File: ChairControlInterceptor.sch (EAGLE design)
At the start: 22 parts, among them J1 Digital_0_7, J2 Analog, J3 Digital_8_13, SW1 TL46WO, X1 INPUT, X2 OUTPUT, X4 INPUT

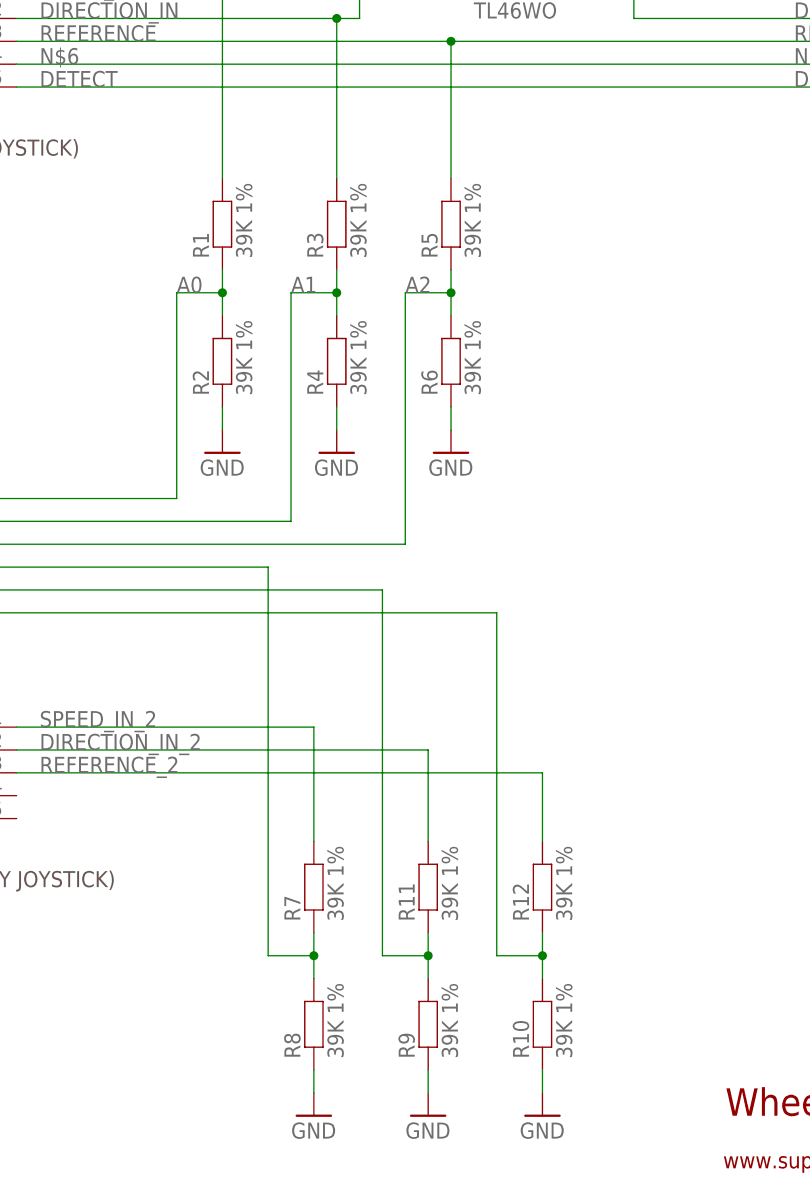
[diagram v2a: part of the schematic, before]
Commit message: Moved Arduino headers to correct location and adjusted connector positions
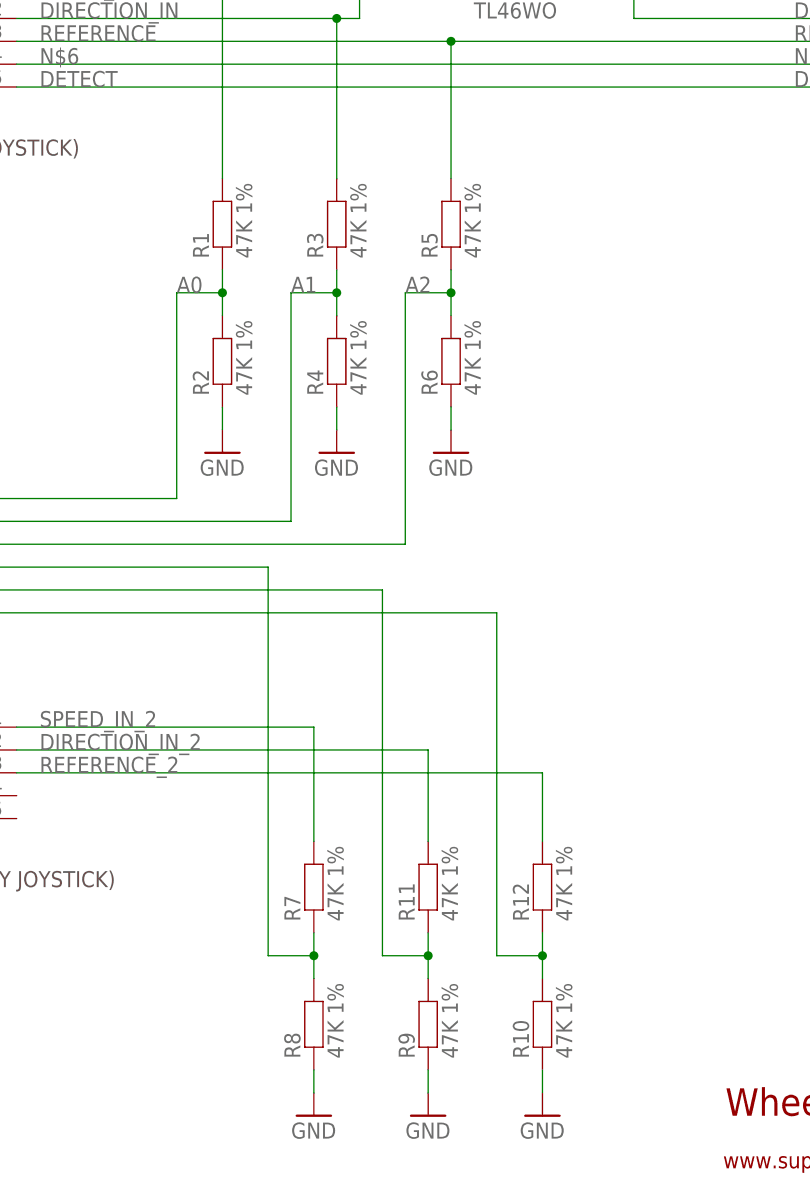
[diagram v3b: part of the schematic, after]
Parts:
- R1, R10, R11, R12, R2, R3, R4, R5, R6, R7, R8, R9: value 39K 1% -> 47K 1%
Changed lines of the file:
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@@
 <part name="X2" library="SparkFun-Connectors" deviceset="DB9" device="FEMALE" value="OUTPUT"/>
 <part name="GND2" library="freetronics" deviceset="GND" device=""/>
-<part name="R1" library="freetronics-jon" deviceset="RESISTOR" device="0603" value="39K 1%"/>
-<part name="R2" library="freetronics-jon" deviceset="RESISTOR" device="0603" value="39K 1%"/>
-<part name="R3" library="freetronics-jon" deviceset="RESISTOR" device="0603" value="39K 1%"/>
-<part name="R4" library="freetronics-jon" deviceset="RESISTOR" device="0603" value="39K 1%"/>
-<part name="R5" library="freetronics-jon" deviceset="RESISTOR" device="0603" value="39K 1%"/>
-<part name="R6" library="freetronics-jon" deviceset="RESISTOR" device="0603" value="39K 1%"/>
+<part name="R1" library="freetronics-jon" deviceset="RESISTOR" device="0603" value="47K 1%"/>
+<part name="R2" library="freetronics-jon" deviceset="RESISTOR" device="0603" value="47K 1%"/>
+<part name="R3" library="freetronics-jon" deviceset="RESISTOR" device="0603" value="47K 1%"/>
+<part name="R4" library="freetronics-jon" deviceset="RESISTOR" device="0603" value="47K 1%"/>
+<part name="R5" library="freetronics-jon" deviceset="RESISTOR" device="0603" value="47K 1%"/>
+<part name="R6" library="freetronics-jon" deviceset="RESISTOR" device="0603" value="47K 1%"/>
 <part name="GND3" library="freetronics" deviceset="GND" device=""/>
 <part name="GND4" library="freetronics" deviceset="GND" device=""/>
@@
 <part name="X4" library="SparkFun-Connectors" deviceset="DB9" device="MALE" value="INPUT"/>
 <part name="GND7" library="freetronics" deviceset="GND" device=""/>
-<part name="R7" library="freetronics-jon" deviceset="RESISTOR" device="0603" value="39K 1%"/>
-<part name="R8" library="freetronics-jon" deviceset="RESISTOR" device="0603" value="39K 1%"/>
+<part name="R7" library="freetronics-jon" deviceset="RESISTOR" device="0603" value="47K 1%"/>
+<part name="R8" library="freetronics-jon" deviceset="RESISTOR" device="0603" value="47K 1%"/>
 <part name="GND8" library="freetronics" deviceset="GND" device=""/>
-<part name="R9" library="freetronics-jon" deviceset="RESISTOR" device="0603" value="39K 1%"/>
-<part name="R10" library="freetronics-jon" deviceset="RESISTOR" device="0603" value="39K 1%"/>
-<part name="R11" library="freetronics-jon" deviceset="RESISTOR" device="0603" value="39K 1%"/>
-<part name="R12" library="freetronics-jon" deviceset="RESISTOR" device="0603" value="39K 1%"/>
+<part name="R9" library="freetronics-jon" deviceset="RESISTOR" device="0603" value="47K 1%"/>
+<part name="R10" library="freetronics-jon" deviceset="RESISTOR" device="0603" value="47K 1%"/>
+<part name="R11" library="freetronics-jon" deviceset="RESISTOR" device="0603" value="47K 1%"/>
+<part name="R12" library="freetronics-jon" deviceset="RESISTOR" device="0603" value="47K 1%"/>
 <part name="GND9" library="freetronics" deviceset="GND" device=""/>
 <part name="GND10" library="freetronics" deviceset="GND" device=""/>
